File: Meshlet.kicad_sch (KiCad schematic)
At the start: 104 parts, among them J1 SWD, J10 GPIO Exp., J11 GPS Header, J12 Thermistor Pins, J13 Ext. Notif. Header, J2 User Btn Header, J3 Batt. Header (Picoblade 1.25), J4 Batt. Header (JST-PH 2.0), J5 USB_C_Receptacle_USB2.0_16P, J6 Ext. Power Header, J7 STEMMA QT I2C, J8 Ext. Power Header, J9 I2C PINHEADER, Q1 AO3400A, SW1 RST, SW2 BOOTSEL, U1 XC6206PxxxMR, U11 INA3221, U2 USBLC6-2SC6, U3 XC6206PxxxMR, U4 RP2350_60QFN, U5 Wio-SX1262, U7 BME280, U8 W25Q32JVZP, U9 XC6206PxxxMR, Y1 12.000MHz

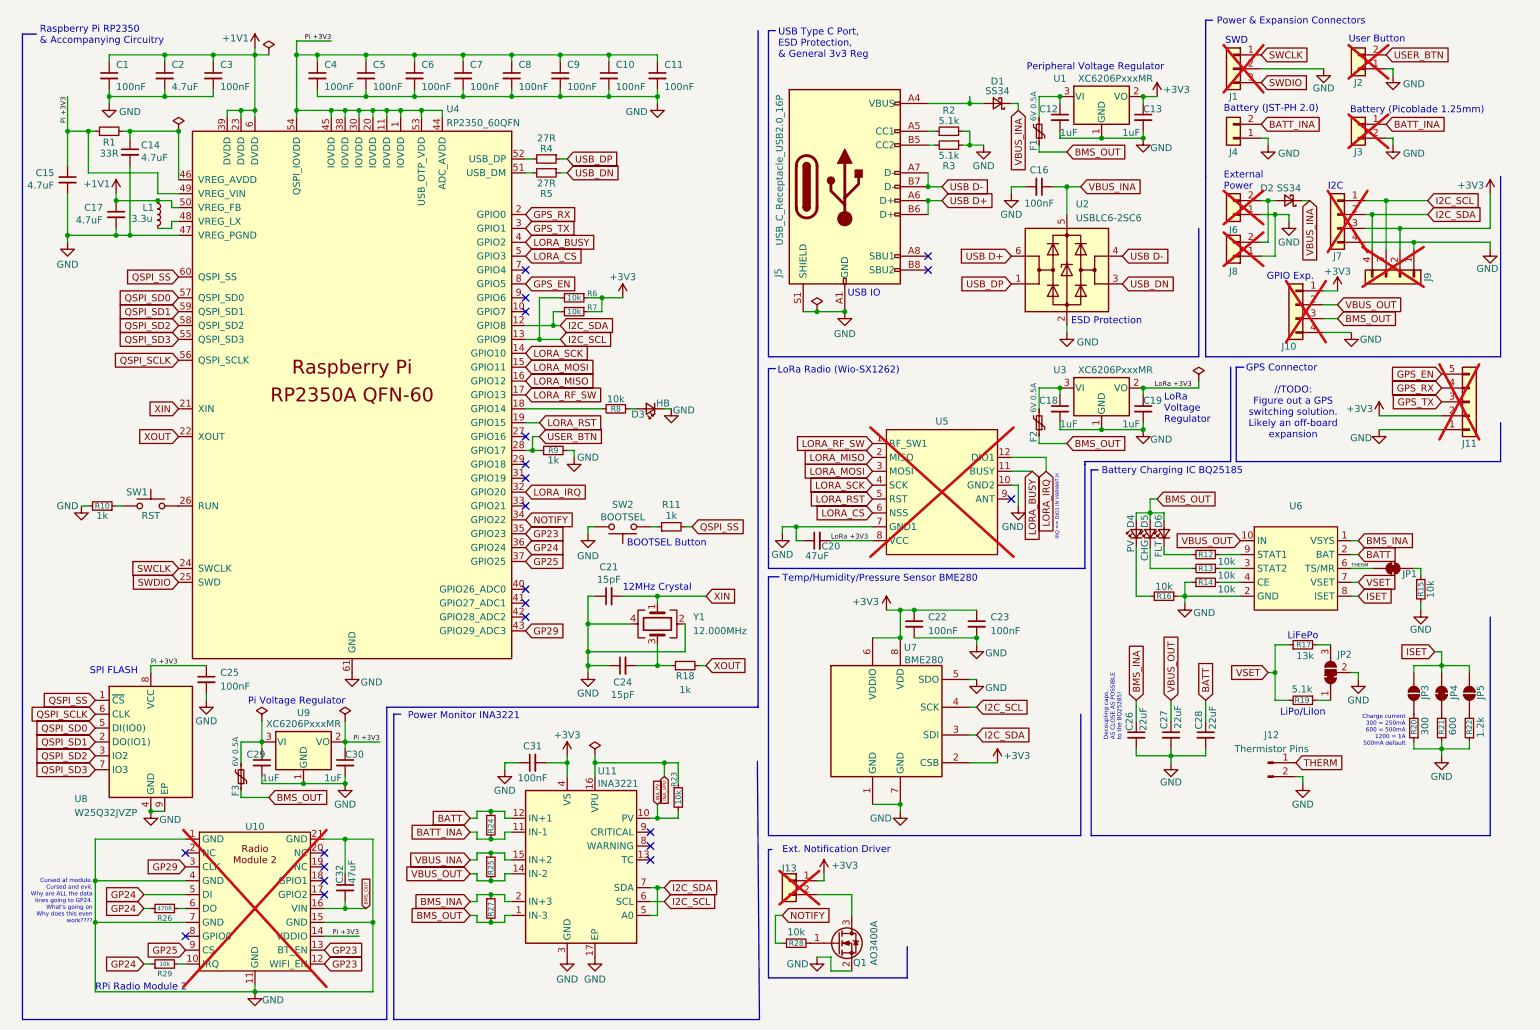
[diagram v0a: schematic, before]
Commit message: Major changes to schematic
Replace BQ24074 with BQ25185, remove extraneous passives, simplified several areas, add extra GPIO breakouts, reannotated schematic, etc.
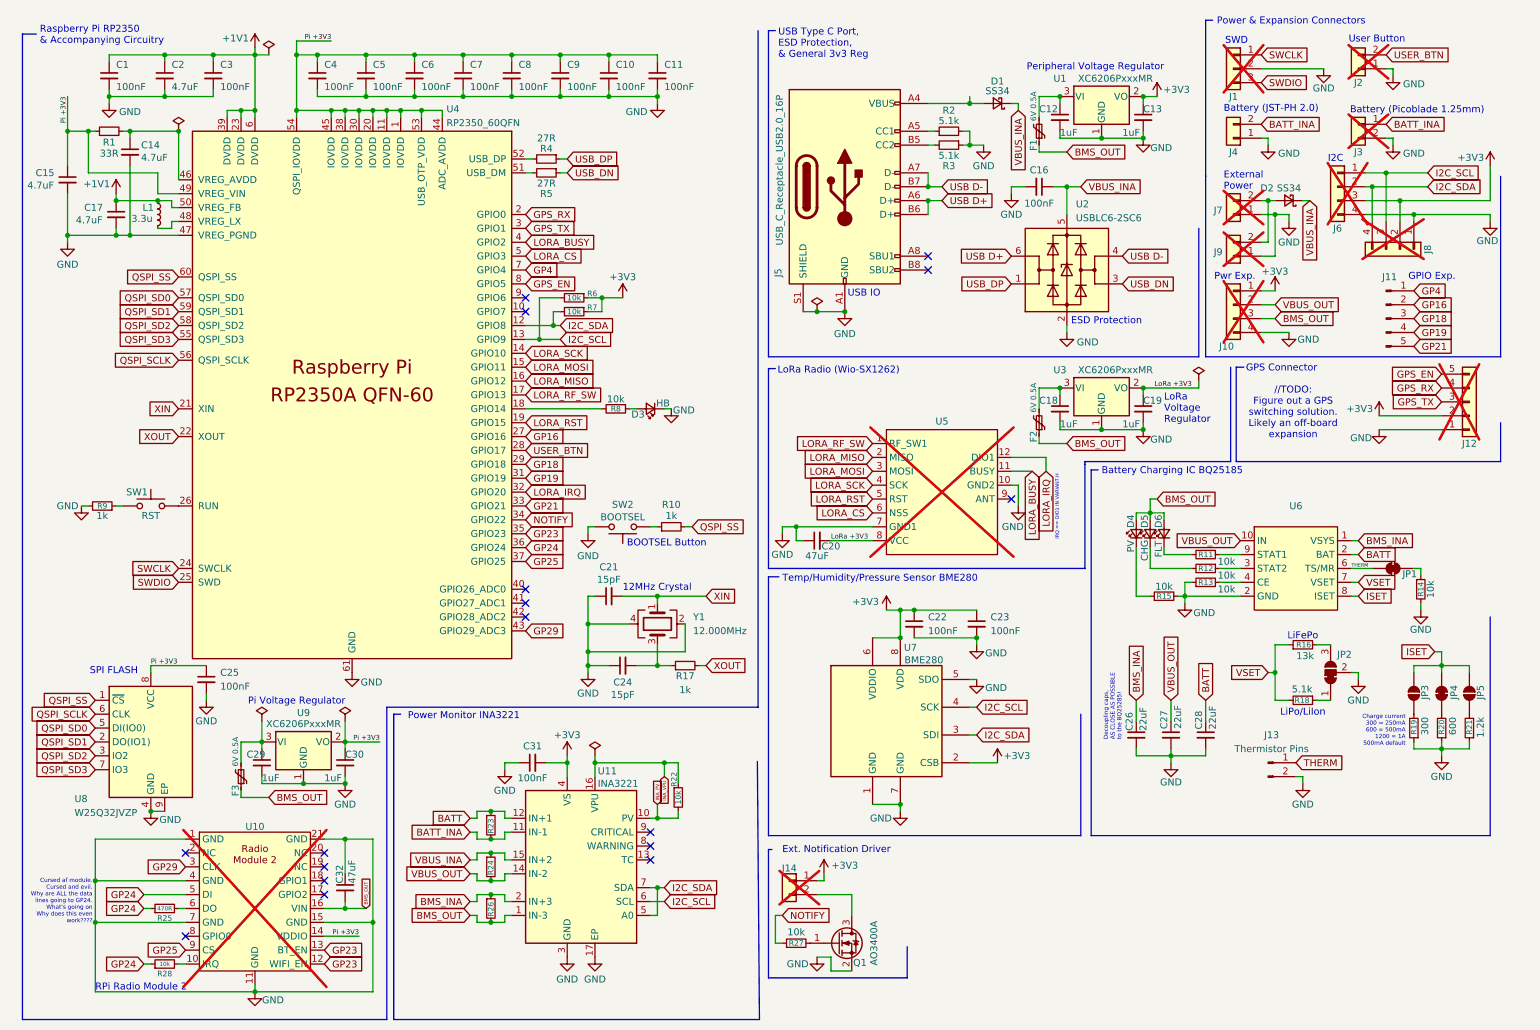
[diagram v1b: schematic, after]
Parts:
- removed R9: 1k, Resistor_SMD:R_0402_1005Metric, symbol Device:R_Small
- added J11: GPIO Exp., symbol Connector:Conn_01x05_Pin
- J10: value GPIO Exp. -> Pwr Exp.
- renumbered J11 to J12, J12 to J13, J13 to J14, J7 to J6, J6 to J7, J9 to J8, J8 to J9, R11 to R10, R12 to R11, R13 to R12, R14 to R13, R15 to R14, R16 to R15, R17 to R16, R18 to R17, R19 to R18, R20 to R19, R21 to R20, R22 to R21, R23 to R22, R24 to R23, R25 to R24, R26 to R25, R27 to R26, R28 to R27, R29 to R28, R10 to R9
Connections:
- net GP16: now reaches U4.27 (GPIO16)
- net GP16: now also J11.2 (Pin_2)
- net GP18: now reaches U4.29 (GPIO18)
- net GP18: now also J11.3 (Pin_3)
- net GP19: now reaches U4.31 (GPIO19)
- net GP19: now also J11.4 (Pin_4)
- net GP21: now reaches U4.33 (GPIO21)
- net GP21: now also J11.5 (Pin_5)
- net GP4: now reaches U4.7 (GPIO4)
- net GP4: now also J11.1 (Pin_1)
- no-connect marks 22 -> 17
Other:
- note added: "Pwr Exp."
- moved on the sheet: J10, J6, J8

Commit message: Redesign!
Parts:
- removed J10: Pwr Exp., Connector_PinHeader_1.27mm:PinHeader_1x04_P1.27mm_Vertical, symbol Connector_Generic:Conn_01x04
- removed J8: I2C PINHEADER, Connector_PinHeader_1.27mm:PinHeader_1x04_P1.27mm_Vertical, symbol Connector_Generic:Conn_01x04
- C26, C27, C28: footprint (none) -> Capacitor_SMD:C_0402_1005Metric
- J1: footprint Connector_JST:JST_SH_SM03B-SRSS-TB_1x03-1MP_P1.00mm_Horizontal -> Connector_PinHeader_1.27mm:PinHeader_1x03_P1.27mm_Vertical
- J11: footprint (none) -> Connector_PinHeader_2.00mm:PinHeader_1x05_P2.00mm_Vertical
- J12: footprint Connector_PinHeader_1.27mm:PinHeader_1x05_P1.27mm_Vertical -> Connector_PinHeader_2.00mm:PinHeader_1x05_P2.00mm_Vertical
- J13: footprint (none) -> Connector_PinHeader_2.54mm:PinHeader_1x02_P2.54mm_Vertical
- J14, J2: footprint Connector_PinHeader_1.27mm:PinHeader_1x02_P1.27mm_Vertical -> Connector_PinHeader_2.00mm:PinHeader_1x02_P2.00mm_Vertical
- J6: footprint Connector_JST:JST_PH_S4B-PH-SM4-TB_1x04-1MP_P2.00mm_Horizontal -> Connector_PinHeader_2.00mm:PinHeader_1x04_P2.00mm_Vertical
- J7: footprint Connector_JST:JST_XH_S2B-XH-A_1x02_P2.50mm_Horizontal -> Connector_JST:JST_PH_S2B-PH-SM4-TB_1x02-1MP_P2.00mm_Horizontal
- JP1, JP4: footprint (none) -> Jumper:SolderJumper-2_P1.3mm_Bridged_RoundedPad1.0x1.5mm
- JP2: footprint (none) -> Jumper:SolderJumper-3_P1.3mm_Bridged12_RoundedPad1.0x1.5mm
- JP3, JP5: footprint (none) -> Jumper:SolderJumper-2_P1.3mm_Open_RoundedPad1.0x1.5mm
- R16, R18, R19, R20, R21: footprint (none) -> Resistor_SMD:R_0402_1005Metric
- U6: value ~ -> BQ25185; footprint (none) -> Package_DFN_QFN:Texas_DLH0010A_WSON-10-1EP_2.2x2mm_P0.4mm_EP0.9x1.5mm_ThermalVias
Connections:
- net BATT_INA: now also J3.2 (Pin_2); no longer J3.1 (Pin_1)
- net GND: now also J3.1 (Pin_1), U6.11 (GND), U6.5 (GND); no longer J3.2 (Pin_2), U6.2 (BAT)
- net GP4: now also U4.8 (GPIO5); no longer U4.7 (GPIO4)
- net GPS_EN: now also U4.7 (GPIO4); no longer U4.8 (GPIO5)
- net I2C_SCL: now also J6.2 (Pin_2); no longer J6.1 (Pin_1)
- net I2C_SDA: now also J6.1 (Pin_1); no longer J6.2 (Pin_2)
- net VBUS_INA: no longer C16.1, U2.5 (VBUS)
- net USB_RAW: now reaches D1.2 (A), J5.A4 (VBUS), J5.A9 (VBUS), J5.B4 (VBUS), J5.B9 (VBUS)
- net USB_RAW: now also C16.1, U2.5 (VBUS)
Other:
- note added: "Battery Charging IC (BQ25185)"
- note added: "Peripheral Voltage Regulator (BME280, INA3221, external peripherals i.e. OLED, cardkb)"
- note added: "Power Monitor (INA3221)"
- note added: "Temp/Humidity/Pressure Sensor (BME280)"
- note removed: "Battery Charging IC BQ25185"
- note removed: "Peripheral Voltage Regulator"
- note removed: "Power Monitor INA3221"
- note removed: "Pwr Exp."
- note removed: "Temp/Humidity/Pressure Sensor BME280"
- moved on the sheet: C32, D1, J3, J6

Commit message: 4 layer ver. complete!
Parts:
- removed J1: SWD, Connector_PinHeader_1.27mm:PinHeader_1x03_P1.27mm_Vertical, symbol Connector_Generic:Conn_01x03
- removed R9: 1k, Resistor_SMD:R_0402_1005Metric, symbol Device:R_Small
- removed SW1: RST, Button_Switch_SMD:SW_Push_1P1T_XKB_TS-1187A, symbol Switch:SW_Push
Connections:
- net +3V3: no longer R6.1, R7.1
- net I2C_SCL: now also J6.1 (Pin_1); no longer J6.2 (Pin_2)
- net I2C_SDA: now also J6.2 (Pin_2); no longer J6.1 (Pin_1)
- net Pi +3V3: now also R6.1, R7.1, U4.26 (RUN)
- net at U4.18 (GPIO14): no longer R8.2
- net HB: now reaches U4.10 (GPIO7)
- net HB: now also R8.2
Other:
- note removed: "SWD"
- moved on the sheet: D2, D3, J11, J4, J7, J9, R6, R7, R8
